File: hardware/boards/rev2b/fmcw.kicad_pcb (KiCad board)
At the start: 4 copper layers, 124.5 x 229.8 mm, 445 parts, among them CON1 BARREL_JACK, J1 SD_Card, J2 USB_B_Micro, J3 SMA, J4 SMA, J5 SMA, J6 Conn_02x08_Odd_Even, Q1 DNP(RE1C002UN), Q2 RE1C002UN, SW1 SW_PUSH, T1 uwave, T10 uwave, T11 uwave, T12 uwave, T13 uwave, T14 uwave, T2 uwave, T3 uwave, T4 uwave, T5 uwave, T6 uwave, T8 uwave, T9 uwave, U1 LP5907MFX-3.3, U10 LP5907MFX-3.0, U11 LTC2292, U12 ADF4158, U13 TLV172DCK, U14 PAT1220-C-3DB, U15 HMC431, U16 PD4859J5050S2HF, U17 PAT1220-C-5DB, U18 SE5004L, U2 LP5907MFX-1.8, U20 PAT1220-C-6DB, U21 LMV321, U22 TRF37A73, U23 SKY65404, U24 TRF37A73, U25 SKY65404, U26 L7980, U27 L7980, U28 L7980, U29 LP2985A-10DBVR, U3 KT2520K-T, U30 TPS7A91, U31 TPS7A91, U32 TPS7A91, U33 LP5907MFX-3.0, U34 TPS7A91, U35 5400BL15B050E, U36 5400BL15B050E, U37 5400BL15B050E, U38 ADL5802, U39 ADA4940-2, U4 NC7SVU04P5X, U40 TPS7A91, U5 NB3N551, U6 XC7A15T-FTG256, U7 W25Q32JV, U8 93LCxxBxxOT, U9 FT2232H, Y1 12MHz

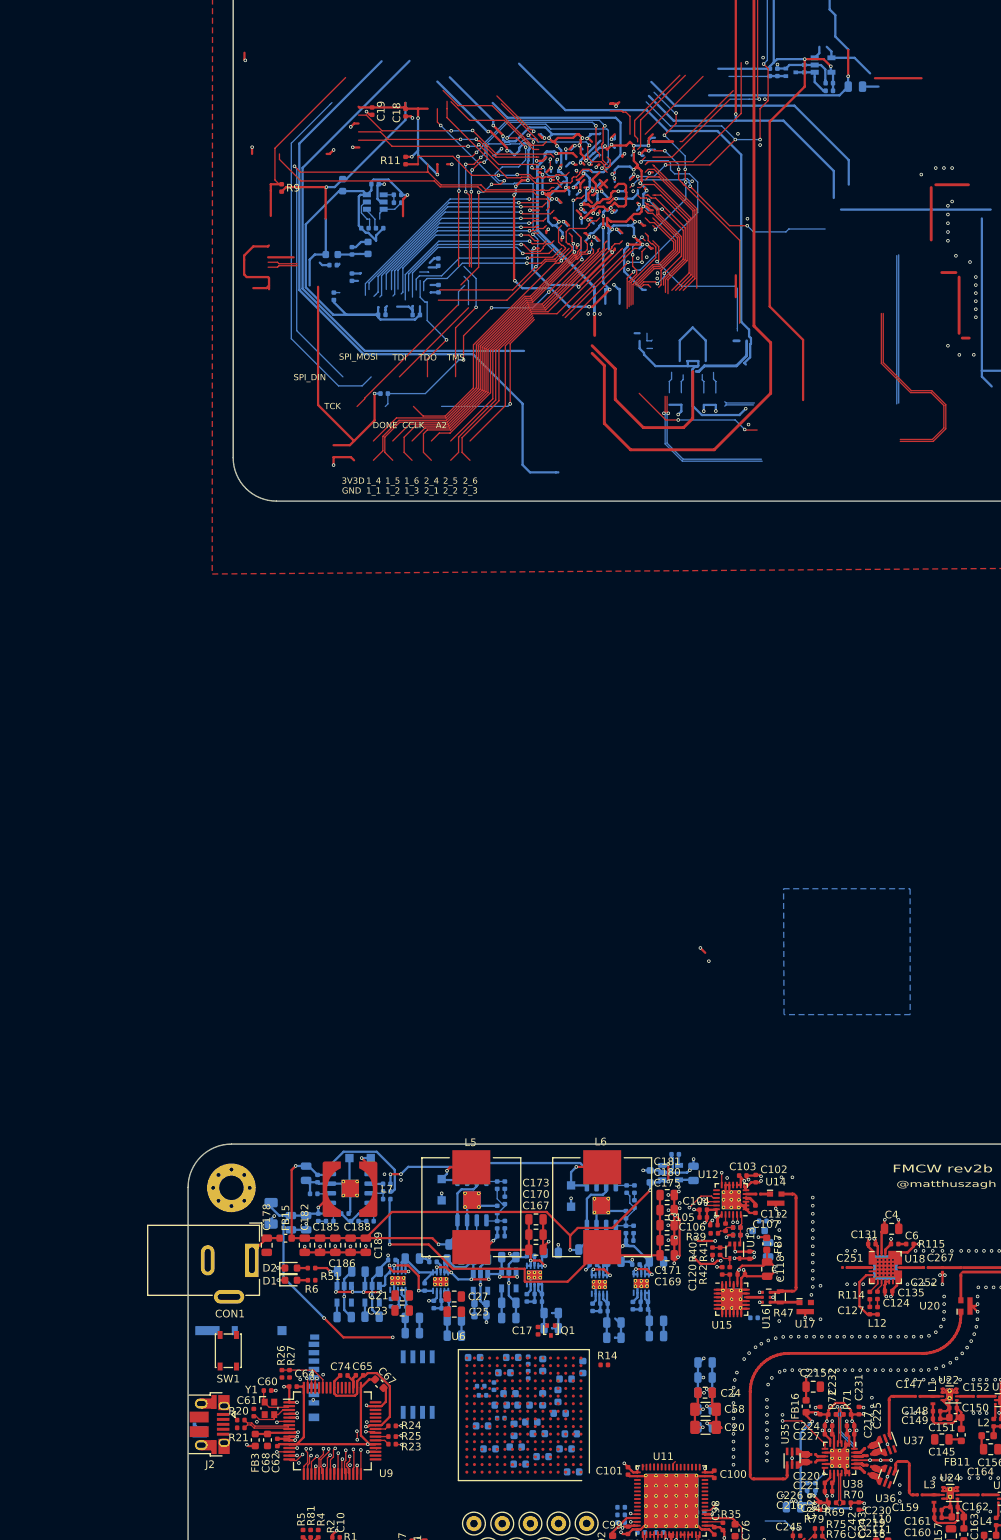
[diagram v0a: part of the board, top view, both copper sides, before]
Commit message: rev2b pcb: replace wilkinson divider with power splitter
Closes #4.
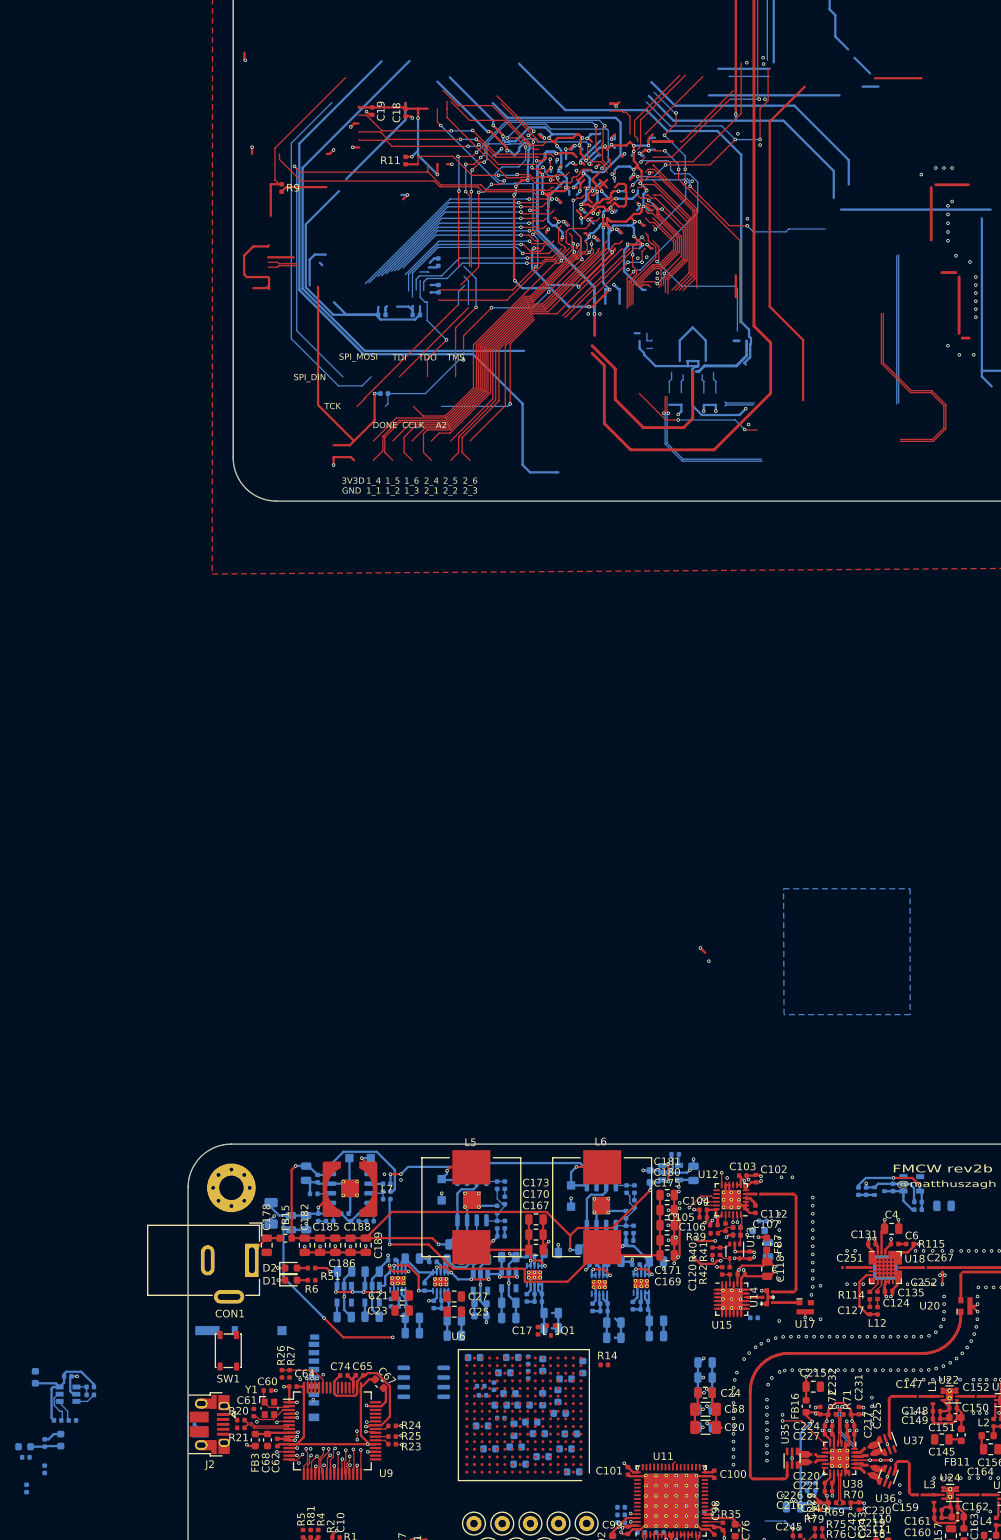
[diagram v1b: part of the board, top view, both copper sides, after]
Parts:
- removed R47: 100, fmcw_v5:R_0603b
- removed the T8 at (167.2, 253.6)
- removed U16: PD4859J5050S2HF, RF_Converter:Anaren_0805_2012Metric-6
- added T7: uwave, fmcw_v5:uwm_0.38_0.17_90, F.Cu at (167.2, 253.6)
- U14: value PAT1220-C-3DB -> PS2012GT2-R50; footprint RF_Converter:RF_Attenuator_Susumu_PAT1220 -> fmcw_v5:Susumu_PS2012GT2-R50
- U17: value PAT1220-C-5DB -> PAT1220-C-2DB
- U7: value W25Q32JV -> MX25L3233F; footprint Package_SO:SOIJ-8_5.3x5.3mm_P1.27mm -> Package_SO:SOP-8_3.9x4.9mm_P1.27mm
- moved C69 161.9 mm to (53.5, 250.6)
- moved C70 161.9 mm to (53.5, 254.1)
- moved R17 161.9 mm to (59.5, 243.3)
- moved R19 161.9 mm to (51.0, 252.5)
- moved R22 161.9 mm to (51.1, 256.6)
- moved R3 161.9 mm to (57.1, 247.7)
- moved C59 161.9 mm to (56.5, 241.9)
- moved C66 161.9 mm to (55.6, 250.3)
- moved FB4 161.9 mm to (50.9, 251.1)
- moved FB5 161.9 mm to (52.3, 242.0)
- moved R18 161.9 mm to (59.5, 244.3)
- moved R82 161.9 mm to (55.2, 247.7)
- moved U8 161.9 mm to (56.6, 244.2)
- moved FB8 147.6 mm to (171.7, 219.5)
- moved U21 147.6 mm to (167.5, 216.6)
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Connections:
- T1 pad 1: Net-(R47-Pad2) -> Net-(C112-Pad1)
- T2 pad 1: Net-(R47-Pad2) -> Net-(C112-Pad1)
- U14 pad 1: Net-(C112-Pad1) -> Net-(U14-Pad1)
- U14 pad 2: Net-(R47-Pad2) -> Net-(U14-Pad2)
- U14 pad 3: GND -> Net-(C112-Pad1)
- U15 pad 16: Net-(U15-Pad16) -> Net-(U14-Pad1)
- U17 pad 1: Net-(R47-Pad1) -> Net-(U14-Pad2)
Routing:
- net Net-(C112-Pad1): track 1.26 -> 18.6 mm
- net Net-(R47-Pad2): track 16.1 -> 0.00 mm
- net /fpga/usb/3V3_IO: track 89.8 -> 82.1 mm
- net /5VPA: track 44.7 -> 38.2 mm, vias 2 -> 1
- net Net-(C127-Pad2): track 22.6 -> 17.9 mm
- net /3V3D: track 276.0 -> 271.3 mm, vias 45 -> 44
- net /fpga/usb/USBDa_P: track 3.89 -> 0.00 mm
- net Net-(R47-Pad1): track 3.89 -> 0.00 mm
- net /3V3A: track 115.0 -> 111.3 mm
- net Net-(U14-Pad2): track 0.00 -> 3.60 mm
- net /fpga/RXF#: track 26.2 -> 22.7 mm
- net /fpga/FT_D6: track 27.5 -> 24.1 mm
- net /fpga/usb/USB_5V: track 3.35 -> 0.00 mm
- net /fpga/TXE#: track 26.0 -> 22.7 mm
- net /fpga/FT_D3: track 31.9 -> 29.1 mm
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
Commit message: rev2 pcb: finish routing traces
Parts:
- added T15: uwave, fmcw_v5:uwm_0.38_0.17_90, F.Cu at (162.3, 83.8)
- added T16: uwave, fmcw_v5:uwm_0.38_0.17_90, F.Cu at (163.4, 79.2)
- C10, C11, C13, C16, C18, C7, C9, FB1, FB2, R1, R11, R2, R4, R5, R81, U3, U4, U5: moved to B.Cu
- C121, C63, C71, C72, C73, FB8, Q2, R43, R44, R45, R46, U21: moved to F.Cu
- moved C41 226.1 mm to (124.1, 109.5)
- moved C44 226.1 mm to (124.1, 107.6)
- moved C22 218.2 mm to (113.0, 90.3), turned to 180 degrees
- moved C38 207.8 mm to (119.9, 108.9)
- moved R22 156.3 mm to (91.3, 105.5), turned to 180 degrees
- moved R19 156.0 mm to (91.2, 101.7)
- moved C70 155.8 mm to (94.0, 103.6)
- moved C69 155.2 mm to (95.5, 101.2), turned to 270 degrees
- moved R81 154.8 mm to (131.9, 114.0)
- moved U5 154.7 mm to (131.6, 117.5)
- moved R5 154.4 mm to (133.4, 115.2), turned to 180 degrees
- moved R4 154.3 mm to (130.9, 114.0)
- moved FB2 154.1 mm to (130.5, 119.9), turned to 0 degrees
- moved C13 153.7 mm to (129.8, 118.0)
- moved U17 153.5 mm to (165.2, 79.8)
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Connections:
- C57 pad 1: /3V3D -> GND
- C57 pad 2: GND -> /3V3D
- R4 pad 1: /ADF_REF -> /FPGA_REF
- R5 pad 1: /FPGA_REF -> /ADC_REF
- R81 pad 1: /ADC_REF -> /ADF_REF
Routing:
- net /fpga/LED: track 23.5 -> 71.6 mm, vias 5 -> 2
- net /ADF_REF: track 99.6 -> 58.1 mm, vias 0 -> 1
- net /1V0: track 125.5 -> 165.7 mm, vias 17 -> 8
- net /fpga/adc/3V0: track 105.3 -> 71.8 mm, vias 5 -> 8
- net /fpga/CCLK: track 71.2 -> 43.9 mm
- net Net-(C5-Pad1): track 72.5 -> 97.9 mm, vias 1 -> 0
- net /fpga/TMS: track 58.8 -> 33.4 mm, vias 6 -> 2
- net /fpga/TCK: track 71.8 -> 46.8 mm, vias 7 -> 4
- net /ADF_CE: track 14.8 -> 39.7 mm, vias 1 -> 0
- net /ADF_CLK: track 14.1 -> 38.6 mm, vias 1 -> 0
- net GND: track 551.8 -> 575.5 mm, vias 410 -> 244
- net /fpga/SPI_MOSI: track 67.9 -> 44.9 mm, vias 0 -> 5
- net /fpga/ADC_SHDN1: track 22.5 -> 45.4 mm
- net /ADC_REF: track 38.5 -> 17.8 mm
- net /fpga/SPI_DIN: track 67.0 -> 47.0 mm, vias 1 -> 5
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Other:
- board size 124.5 x 229.8 mm -> 118.6 x 62 mm

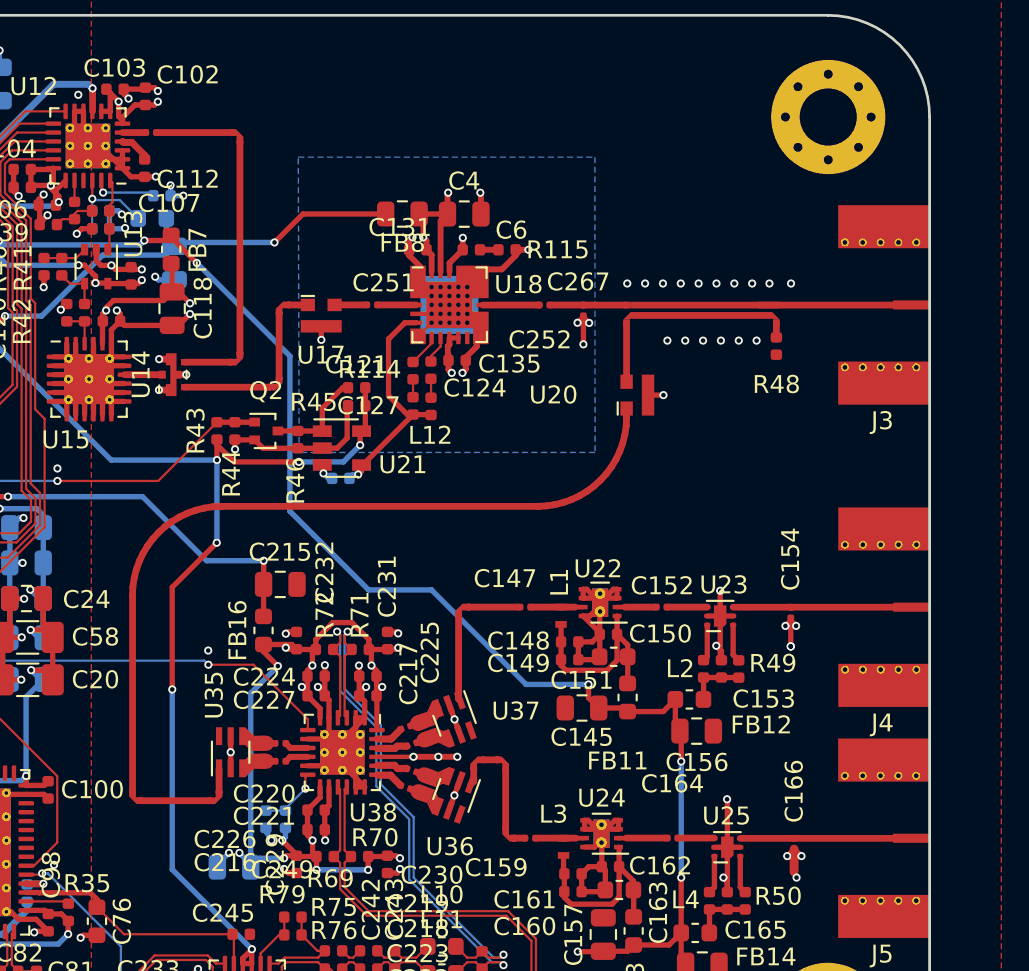
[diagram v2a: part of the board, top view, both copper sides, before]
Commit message: rev2 pcb: place via fences
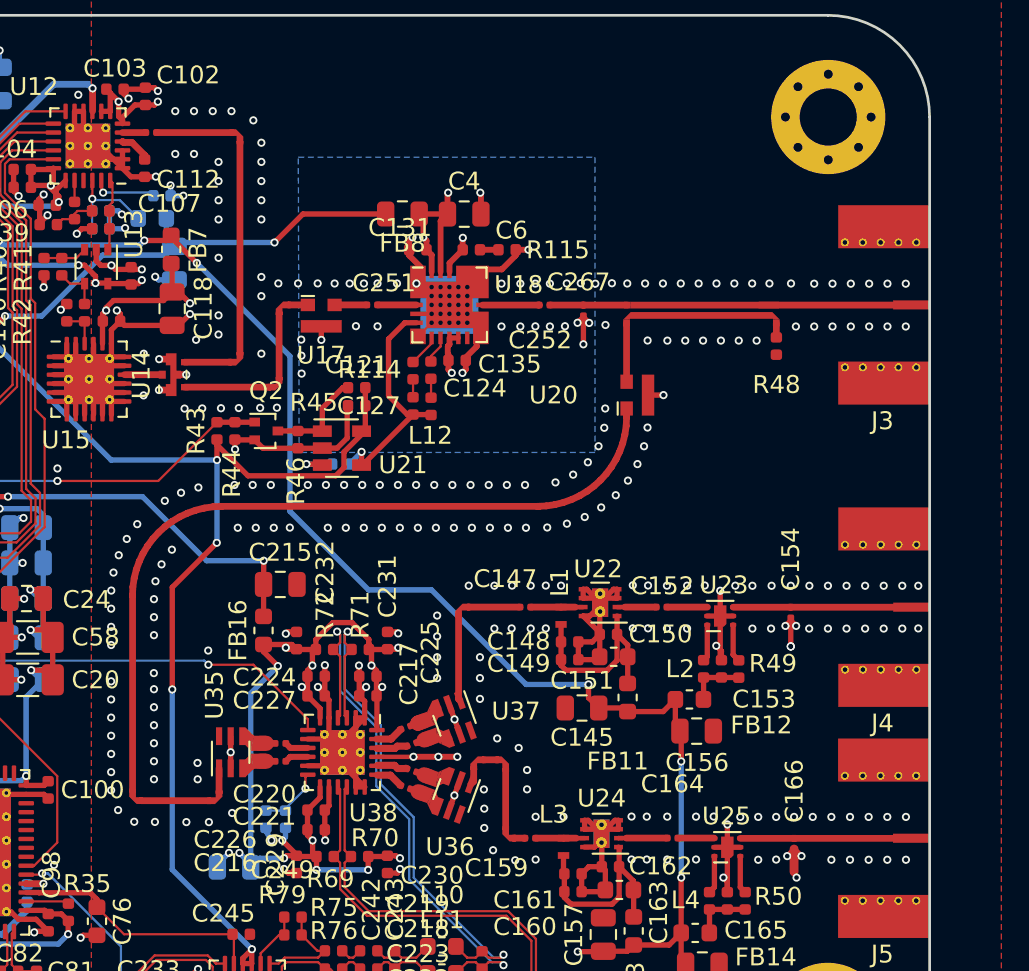
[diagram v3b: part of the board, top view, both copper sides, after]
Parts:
- moved R97 0.80 mm to (166.3, 88.1)
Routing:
- net GND: track 575.5 -> 574.0 mm, vias 244 -> 487
- net Net-(R97-Pad2): track 1.09 -> 2.35 mm
- net /3V3A: track 126.6 -> 127.4 mm, vias 15 -> 13
- net Net-(C127-Pad2): track 13.2 -> 13.7 mm

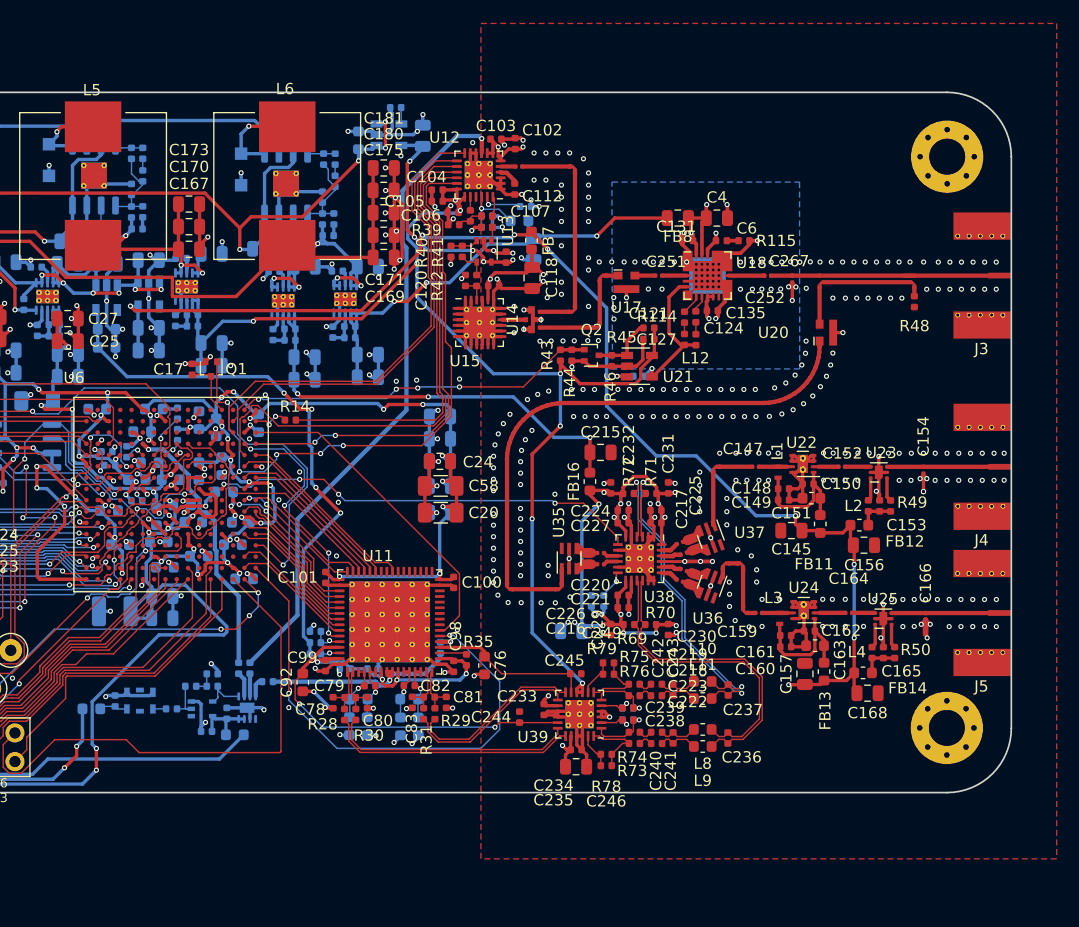
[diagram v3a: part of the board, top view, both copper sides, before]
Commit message: rev2 pcb: add via fences and stitching
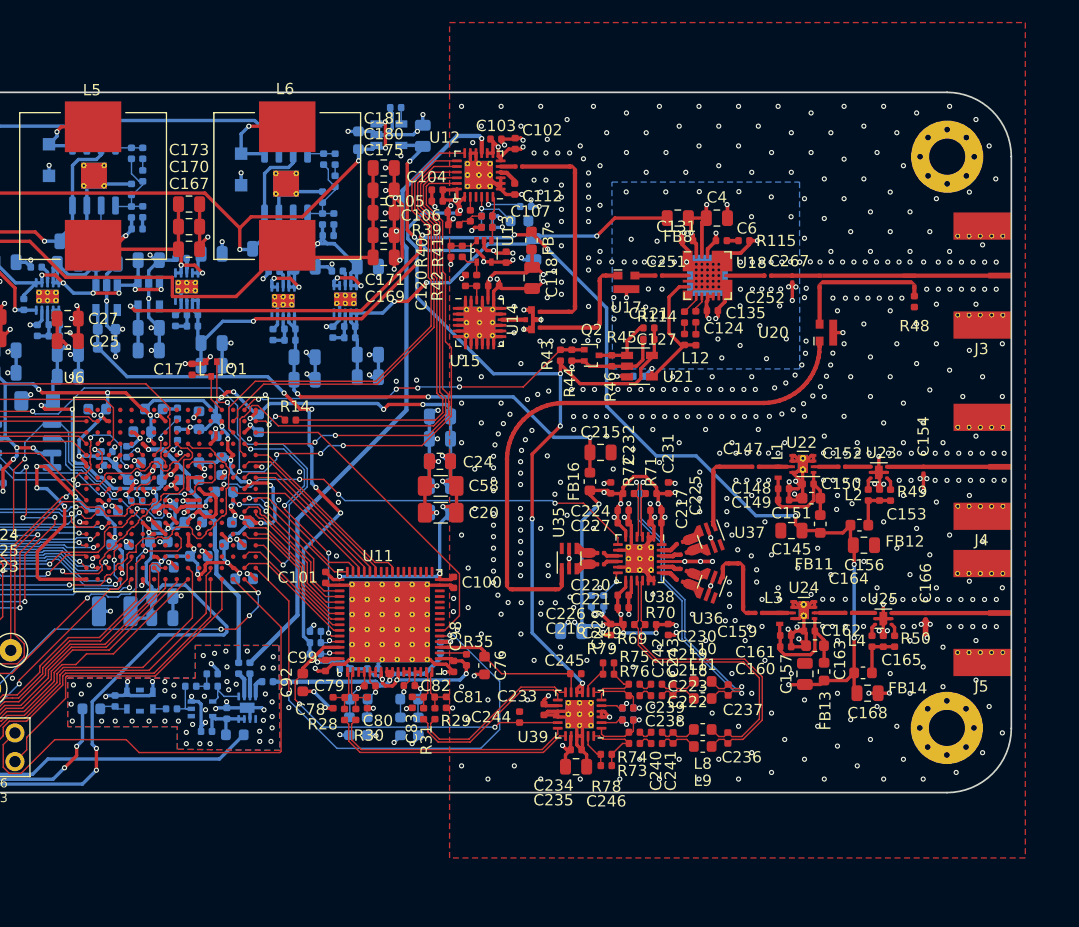
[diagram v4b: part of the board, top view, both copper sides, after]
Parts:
- moved C165 1.01 mm to (188.0, 111.6)
- moved L4 1.01 mm to (187.0, 111.6)
- moved R50 1.01 mm to (189.0, 111.6)
- moved C153 0.96 mm to (187.7, 98.6)
- moved L2 0.96 mm to (186.7, 98.6)
- moved R49 0.96 mm to (188.6, 98.6)
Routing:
- net GND: track 574.0 -> 596.7 mm, vias 487 -> 801
- net Net-(C165-Pad1): track 3.32 -> 4.34 mm
- net Net-(R50-Pad1): track 2.13 -> 1.12 mm
- net Net-(L4-Pad1): track 2.13 -> 1.13 mm
- net Net-(R49-Pad1): track 2.12 -> 1.16 mm
- net Net-(L2-Pad1): track 2.06 -> 1.11 mm
- net Net-(C153-Pad1): track 3.21 -> 4.16 mm
